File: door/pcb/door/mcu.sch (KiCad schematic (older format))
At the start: 28 parts, among them J2 Conn_01x06_Male, J3 DB9_Female_MountingHoles, J4 Conn_01x03_Male, U2 STM32F303CBTx, U3 SN65HVD230, Y1 8 Mhz

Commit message: Taster
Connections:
- net +3V3: now also R2.2; no longer R2.1
- net GND: no longer S1.1, S2.1
- net NRST: no longer S1.3
- net SW2: now also R2.1; no longer R2.2, S2.3
- no-connect marks 30 -> 34
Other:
- moved on the sheet: J2, R2
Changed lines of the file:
@@
 	1    0    0    -1
 $EndComp
-Wire Wire Line
-	3600 4900 4400 4900
-Connection ~ 3600 4900
 $Comp
 L power:GND #PWR02
@@
 L Device:R R2
 U 1 1 5BE9E126
-P 3600 4600
-F 0 "R2" H 3670 4646 50  0000 L CNN
-F 1 "4k7" V 3600 4550 50  0000 L CNN
-F 2 "Resistor_SMD:R_0805_2012Metric" V 3530 4600 50  0001 C CNN
-F 3 "~" H 3600 4600 50  0001 C CNN
-	1    3600 4600
-	1    0    0    -1
-$EndComp
-Wire Wire Line
-	3600 4750 3600 4900
+P 4400 5150
+F 0 "R2" H 4470 5196 50  0000 L CNN
+F 1 "4k7" V 4400 5100 50  0000 L CNN
+F 2 "Resistor_SMD:R_0805_2012Metric" V 4330 5150 50  0001 C CNN
+F 3 "~" H 4400 5150 50  0001 C CNN
+	1    4400 5150
+	1    0    0    -1
+$EndComp
 $Comp
 L power:+3.3V #PWR03
 U 1 1 5BE9EFC8
-P 3600 4450
-F 0 "#PWR03" H 3600 4300 50  0001 C CNN
-F 1 "+3.3V" H 3615 4623 50  0000 C CNN
-F 2 "" H 3600 4450 50  0001 C CNN
-F 3 "" H 3600 4450 50  0001 C CNN
-	1    3600 4450
-	1    0    0    -1
+P 4400 5300
+F 0 "#PWR03" H 4400 5150 50  0001 C CNN
+F 1 "+3.3V" H 4415 5473 50  0000 C CNN
+F 2 "" H 4400 5300 50  0001 C CNN
+F 3 "" H 4400 5300 50  0001 C CNN
+	1    4400 5300
+	-1   0    0    1
 $EndComp
 Wire Wire Line
@@
 Text GLabel 6000 4500 2    50   BiDi ~ 0
 SWIDO
-Wire Wire Line
-	4400 4500 4400 4900
 Wire Wire Line
 	4000 3300 4400 3300
@@
 	1    0    0    -1
 $EndComp
-Text GLabel 4450 5900 2    50   Input ~ 0
+Text GLabel 4400 6050 2    50   Input ~ 0
 SWCLK
-Text GLabel 4450 6000 2    50   BiDi ~ 0
+Text GLabel 4400 6150 2    50   BiDi ~ 0
 SWIDO
 $Comp
 L power:GND #PWR019
 U 1 1 5BE9B0AF
-P 4750 5800
-F 0 "#PWR019" H 4750 5550 50  0001 C CNN
-F 1 "GND" H 4755 5627 50  0000 C CNN
-F 2 "" H 4750 5800 50  0001 C CNN
-F 3 "" H 4750 5800 50  0001 C CNN
-	1    4750 5800
+P 4700 5950
+F 0 "#PWR019" H 4700 5700 50  0001 C CNN
+F 1 "GND" H 4705 5777 50  0000 C CNN
+F 2 "" H 4700 5950 50  0001 C CNN
+F 3 "" H 4700 5950 50  0001 C CNN
+	1    4700 5950
 	0    -1   -1   0
 $EndComp
@@
 L power:+3.3V #PWR0108
 U 1 1 5BEBEC1C
-P 4450 5700
-F 0 "#PWR0108" H 4450 5550 50  0001 C CNN
-F 1 "+3.3V" H 4465 5873 50  0000 C CNN
-F 2 "" H 4450 5700 50  0001 C CNN
-F 3 "" H 4450 5700 50  0001 C CNN
-	1    4450 5700
+P 4400 5850
+F 0 "#PWR0108" H 4400 5700 50  0001 C CNN
+F 1 "+3.3V" H 4415 6023 50  0000 C CNN
+F 2 "" H 4400 5850 50  0001 C CNN
+F 3 "" H 4400 5850 50  0001 C CNN
+	1    4400 5850
 	1    0    0    -1
 $EndComp
@@
 L Connector:Conn_01x06_Male J2
 U 1 1 5BEC0D89
-P 4250 5900
-F 0 "J2" H 4350 5550 50  0000 C CNN
-F 1 "Conn_01x06_Male" H 4350 5450 50  0000 C CNN
-F 2 "Connector_PinHeader_2.54mm:PinHeader_1x06_P2.54mm_Vertical" H 4250 5900 50  0001 C CNN
-F 3 "~" H 4250 5900 50  0001 C CNN
-	1    4250 5900
-	1    0    0    -1
-$EndComp
-Wire Wire Line
-	4750 5800 4450 5800
-Text GLabel 4450 6200 2    50   BiDi ~ 0
+P 4200 6050
+F 0 "J2" H 4300 5700 50  0000 C CNN
+F 1 "Conn_01x06_Male" H 4300 5600 50  0000 C CNN
+F 2 "Connector_PinHeader_2.54mm:PinHeader_1x06_P2.54mm_Vertical" H 4200 6050 50  0001 C CNN
+F 3 "~" H 4200 6050 50  0001 C CNN
+	1    4200 6050
+	1    0    0    -1
+$EndComp
+Wire Wire Line
+	4700 5950 4400 5950
+Text GLabel 4400 6350 2    50   BiDi ~ 0
 NRST
-Text GLabel 4450 6100 2    50   BiDi ~ 0
+Text GLabel 4400 6250 2    50   BiDi ~ 0
 SWO
 Text GLabel 4000 3300 0    50   BiDi ~ 0
@@
 Wire Wire Line
 	6550 2650 6800 2650
-Text Label 4000 4900 0    50   ~ 0
+Text Label 4000 5000 0    50   ~ 0
 SW2
 Text Label 7750 2300 0    50   ~ 0
@@
 Text Label 7750 2400 0    50   ~ 0
 CANL
-$Comp
-L SparkFun-Switches:MOMENTARY-SWITCH-SPST-2-SMD-4.6X2.8MM S2
-U 1 1 5BEEBEDB
-P 3400 4900
-F 0 "S2" H 3400 5335 45  0000 C CNN
-F 1 "SW1" H 3400 5251 45  0000 C CNN
-F 2 "Switches:TACTILE_SWITCH_SMD_4.6X2.8MM" H 3400 5150 20  0001 C CNN
-F 3 "" H 3400 4900 50  0001 C CNN
-F 4 "SWCH-13065" H 3000 5000 60  0000 C CNN "Field4"
-	1    3400 4900
-	1    0    0    -1
-$EndComp
-Wire Wire Line
-	3200 5000 3200 5450
-Wire Wire Line
-	3200 4900 3200 5000
-Connection ~ 3200 5000
-Wire Wire Line
-	3600 4900 3600 5000
-Connection ~ 3600 5000
 Wire Wire Line
 	3600 5000 3600 5100
@@
 	1    0    0    -1
 $EndComp
-Wire Wire Line
-	3350 1300 3350 1400
-Connection ~ 3350 1400
-Wire Wire Line
-	2950 1300 2950 1400
-Connection ~ 2950 1400
 NoConn ~ 4400 4400
 NoConn ~ 4400 4300
@@
 NoConn ~ 5700 3800
 NoConn ~ 5700 4100
+Wire Wire Line
+	3200 5000 3200 5450
+$Comp
+L SparkFun-Switches:MOMENTARY-SWITCH-SPST-2-SMD-4.6X2.8MM S2
+U 1 1 5BEEBEDB
+P 3400 4900
+F 0 "S2" H 3400 5335 45  0000 C CNN
+F 1 "SW1" H 3400 5251 45  0000 C CNN
+F 2 "Switches:TACTILE_SWITCH_SMD_4.6X2.8MM" H 3400 5150 20  0001 C CNN
+F 3 "" H 3400 4900 50  0001 C CNN
+F 4 "SWCH-13065" H 3000 5000 60  0000 C CNN "Field4"
+	1    3400 4900
+	1    0    0    -1
+$EndComp
+Wire Wire Line
+	4400 5000 3600 5000
+Wire Wire Line
+	4400 4500 4400 5000
+Connection ~ 3600 5000
+Connection ~ 4400 5000
+NoConn ~ 3200 4900
+NoConn ~ 3600 4900
+NoConn ~ 2950 1300
+NoConn ~ 3350 1300
 $EndSCHEMATC

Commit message: recplaced usb micro jack with barrel-jack, reworked pcb layout
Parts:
- TP1, TP2: footprint TestPoint:TestPoint_Loop_D1.80mm_Drill1.0mm_Beaded -> TestPoint:TestPoint_Pad_D1.0mm
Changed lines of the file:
@@
 	9100 2300 9650 2300
 Wire Wire Line
-	8350 1950 9100 1950
-Wire Wire Line
 	9100 2850 9100 2500
 Wire Wire Line
 	9100 2500 9650 2500
-Wire Wire Line
-	8350 2850 9100 2850
 Wire Wire Line
 	9650 2800 9650 3000
@@
 F 0 "TP2" V 6745 2724 50  0000 C CNN
 F 1 "TP_CAN_RX" V 6654 2724 50  0000 C CNN
-F 2 "TestPoint:TestPoint_Loop_D1.80mm_Drill1.0mm_Beaded" H 6750 2650 50  0001 C CNN
+F 2 "TestPoint:TestPoint_Pad_D1.0mm" H 6750 2650 50  0001 C CNN
 F 3 "~" H 6750 2650 50  0001 C CNN
 	1    6550 2650
@@
 F 0 "TP1" V 6695 2124 50  0000 C CNN
 F 1 "TP_CAN_TX" V 6604 2124 50  0000 C CNN
-F 2 "TestPoint:TestPoint_Loop_D1.80mm_Drill1.0mm_Beaded" H 6700 2050 50  0001 C CNN
+F 2 "TestPoint:TestPoint_Pad_D1.0mm" H 6700 2050 50  0001 C CNN
 F 3 "~" H 6700 2050 50  0001 C CNN
 	1    6500 2050
@@
 NoConn ~ 2950 1300
 NoConn ~ 3350 1300
+Wire Wire Line
+	8350 1950 9100 1950
+Wire Wire Line
+	8350 2850 9100 2850
 $EndSCHEMATC

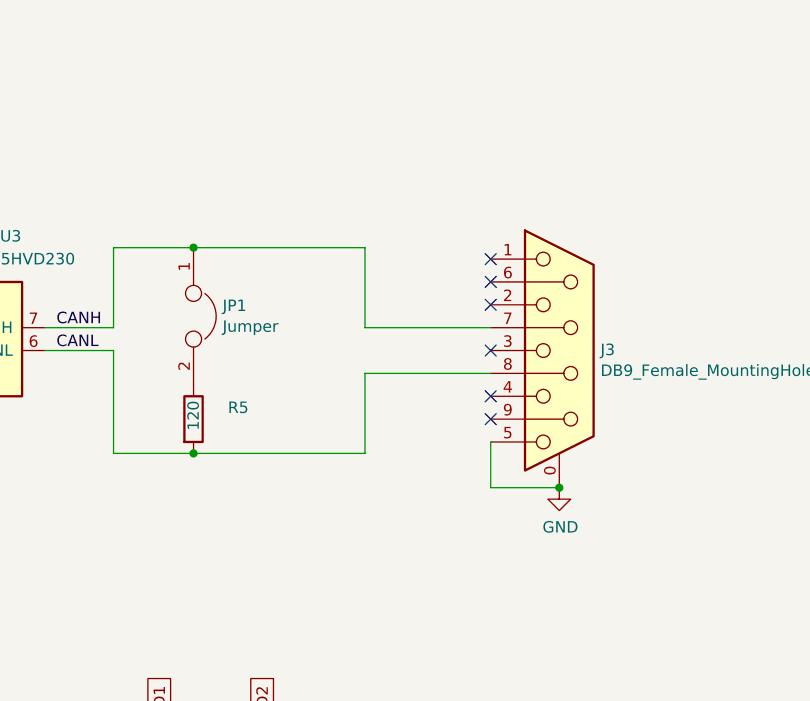
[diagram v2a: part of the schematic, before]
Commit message: changed pinout of DB-9 connector
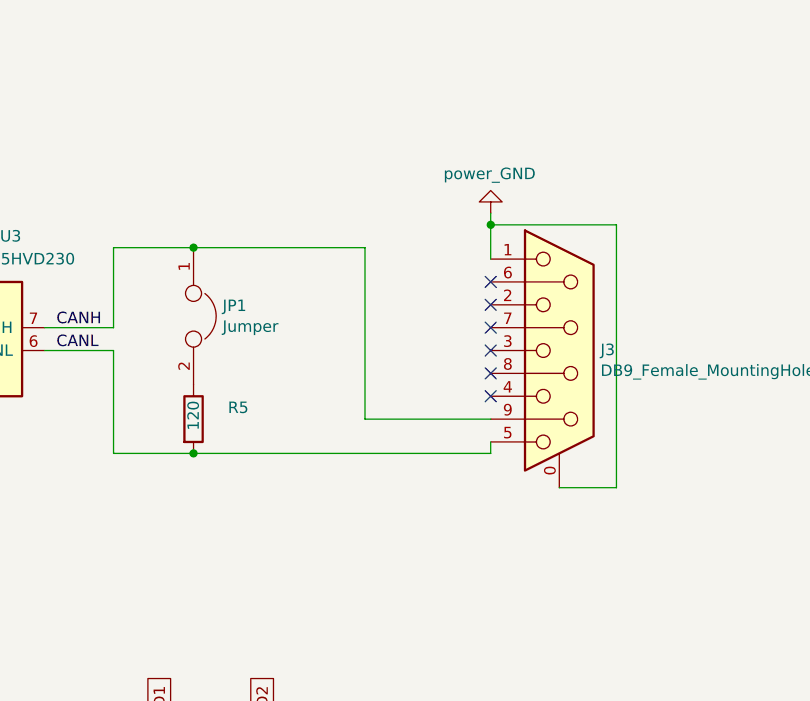
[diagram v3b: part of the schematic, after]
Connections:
- net CANH: now also J3.9; no longer J3.7
- net CANL: now also J3.5; no longer J3.8
- net GND: now also J3.1; no longer J3.5
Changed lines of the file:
@@
 SLEEP
-$Comp
-L Connector:DB9_Female_MountingHoles J3
-U 1 1 5BE8AC5C
-P 9950 2400
-F 0 "J3" H 10130 2403 50  0000 L CNN
-F 1 "DB9_Female_MountingHoles" H 10130 2312 50  0000 L CNN
-F 2 "Connector_Dsub:DSUB-9_Female_Horizontal_P2.77x2.84mm_EdgePinOffset4.94mm_Housed_MountingHolesOffset7.48mm" H 9950 2400 50  0001 C CNN
-F 3 " ~" H 9950 2400 50  0001 C CNN
-	1    9950 2400
-	1    0    0    -1
-$EndComp
-Wire Wire Line
-	9100 1950 9100 2300
-Wire Wire Line
-	9100 2300 9650 2300
-Wire Wire Line
-	9100 2850 9100 2500
-Wire Wire Line
-	9100 2500 9650 2500
-Wire Wire Line
-	9650 2800 9650 3000
-Wire Wire Line
-	9650 3000 9950 3000
-$Comp
-L power:GND #PWR015
-U 1 1 5BE8E40E
-P 9950 3000
-F 0 "#PWR015" H 9950 2750 50  0001 C CNN
-F 1 "GND" H 9955 2827 50  0000 C CNN
-F 2 "" H 9950 3000 50  0001 C CNN
-F 3 "" H 9950 3000 50  0001 C CNN
-	1    9950 3000
-	1    0    0    -1
-$EndComp
-Connection ~ 9950 3000
 $Comp
 L power:VDD #PWR017
@@
 Wire Wire Line
 	8750 5400 8750 5450
-NoConn ~ 9650 2700
 NoConn ~ 9650 2600
 NoConn ~ 9650 2400
 NoConn ~ 9650 2200
 NoConn ~ 9650 2100
-NoConn ~ 9650 2000
 $Comp
 L Connector:TestPoint TP2
@@
 Wire Wire Line
 	8350 1950 9100 1950
-Wire Wire Line
-	8350 2850 9100 2850
+$Comp
+L Connector:DB9_Female_MountingHoles J3
+U 1 1 5BE8AC5C
+P 9950 2400
+F 0 "J3" H 10130 2403 50  0000 L CNN
+F 1 "DB9_Female_MountingHoles" H 10130 2312 50  0000 L CNN
+F 2 "Connector_Dsub:DSUB-9_Female_Horizontal_P2.77x2.84mm_EdgePinOffset4.94mm_Housed_MountingHolesOffset7.48mm" H 9950 2400 50  0001 C CNN
+F 3 " ~" H 9950 2400 50  0001 C CNN
+	1    9950 2400
+	1    0    0    -1
+$EndComp
+Wire Wire Line
+	9650 2850 9650 2800
+Wire Wire Line
+	8350 2850 9650 2850
+Wire Wire Line
+	9650 2700 9100 2700
+Wire Wire Line
+	9100 1950 9100 2700
+NoConn ~ 9650 2300
+NoConn ~ 9650 2500
+$Comp
+L door-cache:power_GND #PWR?
+U 1 1 5C5FE0A1
+P 9650 1800
+F 0 "#PWR?" H 9650 1550 50  0001 C CNN
+F 1 "power_GND" H 9655 1627 50  0000 C CNN
+F 2 "" H 9650 1800 50  0001 C CNN
+F 3 "" H 9650 1800 50  0001 C CNN
+	1    9650 1800
+	-1   0    0    1
+$EndComp
+Wire Wire Line
+	9650 1800 9650 1850
+Wire Wire Line
+	9950 3000 10200 3000
+Wire Wire Line
+	10200 3000 10200 1850
+Wire Wire Line
+	10200 1850 9650 1850
+Connection ~ 9650 1850
+Wire Wire Line
+	9650 1850 9650 2000
 $EndSCHEMATC

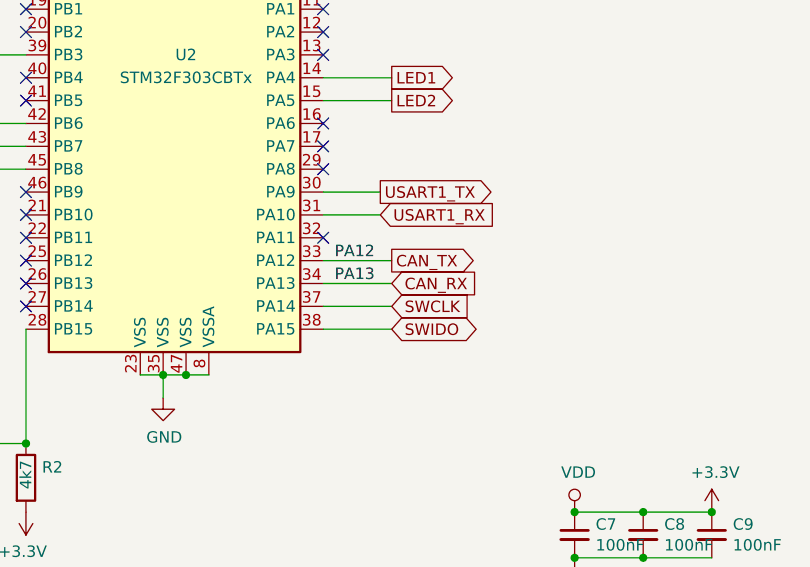
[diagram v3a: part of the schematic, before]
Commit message: corrected error in Layout swido was connected with Can Rx
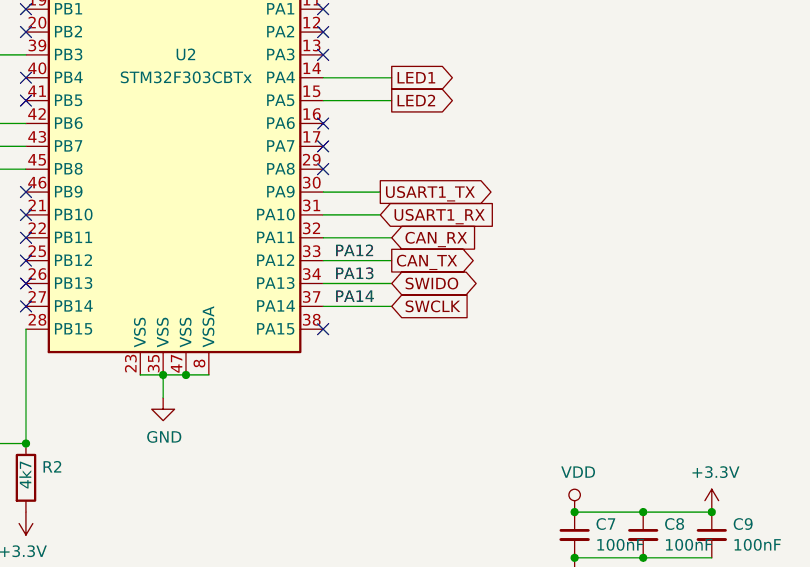
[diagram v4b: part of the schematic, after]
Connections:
- net CAN_RX: now also U2.32 (PA11); no longer U2.34 (PA13)
- net SWIDO: now also U2.34 (PA13); no longer U2.38 (PA15)
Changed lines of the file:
@@
 	6000 4200 5700 4200
-Wire Wire Line
-	6000 4300 5700 4300
 Wire Wire Line
 	6700 2200 6800 2200
@@
 Text GLabel 6000 4200 2    50   Output ~ 0
 CAN_TX
-Text GLabel 6000 4300 2    50   Input ~ 0
+Text GLabel 6000 4100 2    50   Input ~ 0
 CAN_RX
 Text Label 5750 4200 0    50   ~ 0
@@
 Wire Wire Line
 	6000 4400 5700 4400
-Wire Wire Line
-	6000 4500 5700 4500
 Text GLabel 6000 4400 2    50   Input ~ 0
 SWCLK
-Text GLabel 6000 4500 2    50   BiDi ~ 0
+Text GLabel 6000 4300 2    50   BiDi ~ 0
 SWIDO
 Wire Wire Line
@@
 NoConn ~ 5700 3700
 NoConn ~ 5700 3800
-NoConn ~ 5700 4100
 Wire Wire Line
 	3200 5000 3200 5450
@@
 Wire Wire Line
 	9650 1850 9650 2000
+Wire Wire Line
+	5700 4100 6000 4100
+Wire Wire Line
+	5700 4300 6000 4300
+NoConn ~ 5700 4500
+Text Label 5750 4400 0    50   ~ 0
+PA14
 $EndSCHEMATC
